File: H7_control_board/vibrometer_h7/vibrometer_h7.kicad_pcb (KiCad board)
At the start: 4 copper layers, 69.5 x 69.5 mm, 207 parts, among them J201 Conn_01x04_Socket, J202 Conn_02x06, J204 TC2030-NL, J301 USB_C_Receptacle_USB2.0_16P, J501 debug_conn, J601 Conn_01x08_Socket, J701 Conn_01x08_Socket, J801 Conn_01x08_Socket, J901 PH-313D, Q1001 NTR4170N, Q1002 NTR4170N, Q1003 NTR4170N, Q201 BSS138, Q202 BSS138, Q203 BSS138, SW201 SW_Push, SW501 SW_Push, SW502 SW_Push, U201 STM32H723VGTx, U301 USBLC6-2SC6, U302 MT9700, U303 AMS1117-3V3, U901 RC4580, U902 TPA6111A2, Y201 24MHz

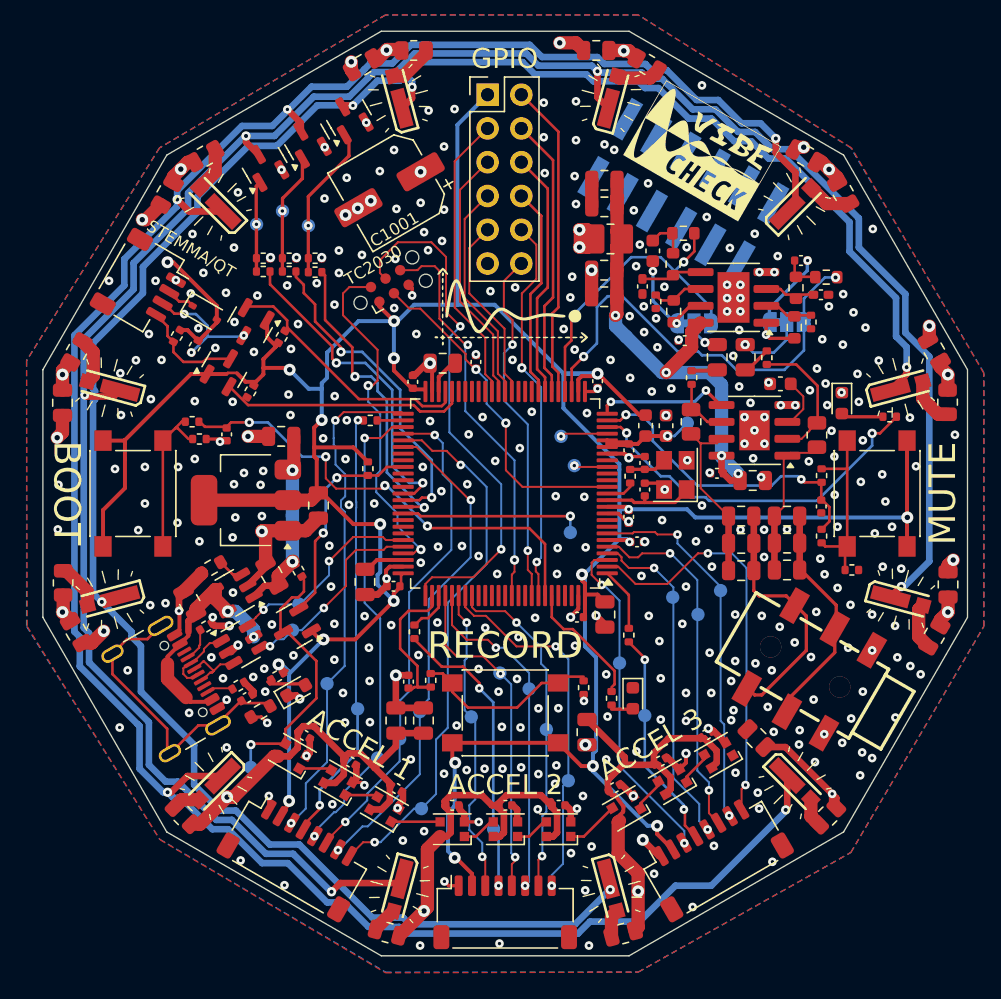
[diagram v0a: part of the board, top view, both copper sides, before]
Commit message: updated logo with ground plane detail
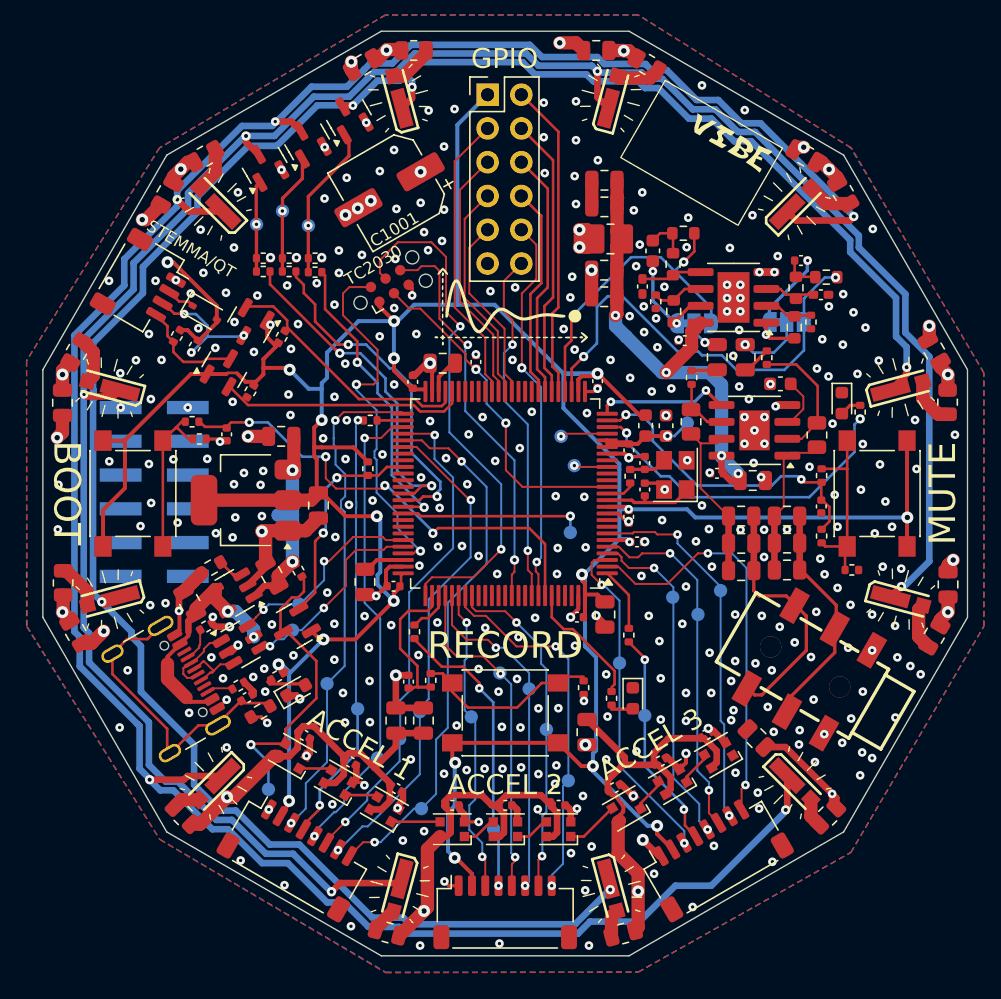
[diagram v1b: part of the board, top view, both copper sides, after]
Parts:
- G*** (x2): value LOGO -> VIBE_RESPONSE_SILKSCREEN; footprint LOGO -> footprints:VIBE_RESPONSE_SILKSCREEN
- G***: value LOGO -> VIBE_CHECK_LOGO; footprint LOGO -> footprints:VIBE_CHECK_LOGO
- G***: value LOGO -> VIBE_CHECK_LOGO_SILKSCREEN; footprint LOGO -> footprints:VIBE_CHECK_LOGO_SILKSCREEN
- moved G*** 52.3 mm to (176.0, 105.0)
- moved J501 45.8 mm to (123.6, 99.9), turned to 180 degrees
- moved G*** 35.7 mm to (139.3, 103.9)
- moved R505 2.25 mm to (176.7, 93.9), turned to 90 degrees
- moved TP201 2.12 mm to (132.2, 122.2)
- moved TP302 1.06 mm to (132.9, 101.6)
- moved G*** 0.16 mm to (164.8, 74.4)
- moved C1010 0.06 mm to (117.7, 110.5)
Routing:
- net /STROBE/FET2_D: track 178.4 -> 187.0 mm
- net /MCU/MUTE_INDICATOR: track 27.6 -> 25.3 mm
- net GND: track 90.0 -> 87.8 mm
- net /ACCEL/LED_ACCEL: track 19.9 -> 22.1 mm
- net /MCU/LED_STROBE_2: track 24.4 -> 25.6 mm
- net /MCU/SWD_DIO: track 26.5 -> 27.7 mm
- net Net-(D502-A): track 3.19 -> 2.07 mm
- net /MCU/LED_STROBE_1: track 24.4 -> 25.4 mm
- net /MCU/LED_STROBE_3: track 23.3 -> 22.5 mm
- net /STROBE/FET3_D: track 167.5 -> 166.7 mm
- net /STROBE/FET1_D: track 171.6 -> 170.8 mm
- net +5V: track 192.5 -> 192.1 mm, vias 19 -> 18
- net +3V3: track 262.0 -> 262.4 mm, vias 18 -> 19

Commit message: boards sent to JLCPCB!
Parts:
- JP901: value FILT BYPASS 2 -> FILT2 BYPASS
- JP902: value FILT BYPASS 1 -> FILT1 BYPASS
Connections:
- net Net-(JP901-A) renamed /AUDIO/FILT2_OUT
- net Net-(JP902-A) renamed /AUDIO/FILT1_OUT
- J601 pad 5: /ACCEL/ACCEL.MISO1 -> /ACCEL/ACCEL.MOSI1
- J601 pad 6: /ACCEL/ACCEL.MOSI1 -> /ACCEL/ACCEL.MISO1
- J701 pad 5: /ACCEL/ACCEL.MISO2 -> /ACCEL/ACCEL.MOSI2
- J701 pad 6: /ACCEL/ACCEL.MOSI2 -> /ACCEL/ACCEL.MISO2
- J801 pad 5: /ACCEL/ACCEL.MISO3 -> /ACCEL/ACCEL.MOSI3
- J801 pad 6: /ACCEL/ACCEL.MOSI3 -> /ACCEL/ACCEL.MISO3
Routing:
- net /ACCEL/ACCEL.MOSI1: track 37.6 -> 38.4 mm
- net /ACCEL/ACCEL.MOSI3: track 27.0 -> 27.6 mm
- net +3V3: track 262.4 -> 262.6 mm, vias 19 -> 18
- net GND: vias 365 -> 366
